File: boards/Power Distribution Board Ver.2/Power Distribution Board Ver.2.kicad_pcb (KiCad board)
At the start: 4 copper layers, 12.4 x 13.7 mm, 93 parts, among them J1 Screw_Terminal_01x02, J2 Screw_Terminal_01x06, J3 Screw_Terminal_01x06, J4 Screw_Terminal_01x06, K1 Relay, K2 Relay, K3 Relay, K4 Relay, K5 Relay, K6 Relay, SW1 SW_Push_Open, U1 SIC431AED-T1-GE3, U2 SIC431AED-T1-GE3, U3 SIC431AED-T1-GE3

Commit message: PCB update 1
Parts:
- C1, C10, C11, C12, C13, C14, C15, C16, C18, C19, C2, C20, C21, C22, C23, C24, C25, C26, C27, C28, C29, C3, C30, C31, C32, C33, C34, C35, C36, C37, C38, C39, C4, C5, C6, C7, C8, C9, J1, J2, J3, J4: moved to B.Cu
- moved D8 166.7 mm to (83.0, 137.4), turned to -90 degrees
- moved C3 157.2 mm to (44.0, 67.7), turned to -90 degrees
- moved C22 150.0 mm to (84.0, 125.7), turned to 180 degrees
- moved C23 145.5 mm to (84.0, 122.7), turned to 180 degrees
- moved C19 142.1 mm to (83.9, 119.7), turned to 180 degrees
- moved C33 138.6 mm to (44.0, 107.7), turned to 180 degrees
- moved C34 138.6 mm to (44.0, 110.7), turned to 180 degrees
- moved C37 138.6 mm to (44.0, 119.7), turned to 180 degrees
- moved C38 138.6 mm to (44.0, 122.7), turned to 180 degrees
- moved C39 138.6 mm to (44.0, 125.7), turned to 180 degrees
- moved C35 138.5 mm to (44.0, 113.7), turned to 180 degrees
- moved C36 138.5 mm to (44.0, 116.7), turned to 180 degrees
- moved C24 137.6 mm to (84.0, 116.7), turned to 180 degrees
- moved C2 135.4 mm to (64.0, 64.0), turned to -90 degrees
- moved C25 133.3 mm to (83.9, 113.7), turned to 180 degrees
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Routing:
- net /E-stop: track 0.00 -> 83.8 mm
- net /V_BAT_IN: track 0.00 -> 21.9 mm
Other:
- board size 12.4 x 13.7 mm -> 127 x 127 mm

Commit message: Edit PCB
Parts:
- C19, C20, C21, C22, C23, C24, C25, C26, C27, C28, C29, C30, C31, C32, C33, C34, C35, C36, C37, C38, C39: moved to F.Cu
- moved J2 119.2 mm to (144.8, 46.8), turned to -90 degrees
- moved J3 88.9 mm to (147.3, 139.7), turned to 180 degrees
- moved D3 63.4 mm to (134.7, 68.8), turned to 0 degrees
- moved D4 40.5 mm to (121.9, 129.9), turned to -90 degrees
- moved D2 28.9 mm to (154.9, 129.6)
- moved D5 19.7 mm to (134.7, 88.9)
- moved C1 16.5 mm to (73.7, 71.1), turned to 0 degrees
- moved D1 15.2 mm to (134.7, 50.6)
- moved K6 15.0 mm to (111.8, 117.1), turned to 180 degrees
- moved K4 13.0 mm to (127.0, 116.8), turned to 180 degrees
- moved C33 12.6 mm to (54.9, 101.6), turned to 0 degrees
- moved C34 12.6 mm to (54.9, 104.6), turned to 0 degrees
- moved C37 12.6 mm to (54.9, 113.6), turned to 0 degrees
- moved C38 12.6 mm to (54.9, 116.6), turned to 0 degrees
- moved C39 12.6 mm to (54.9, 119.6), turned to 0 degrees
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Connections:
- D7 pad 2: /5V_OUT_1 -> /5V_OUT_2
- D9 pad 2: /5V_OUT_1 -> /5V_OUT_3
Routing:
- net /V_BAT_IN: track 21.9 -> 272.3 mm
- net GND: track 0.00 -> 147.7 mm
- net /E-stop: track 83.8 -> 169.8 mm
- net Net-(D9-A): track 0.00 -> 48.7 mm
- net /12V_IN_4: track 0.00 -> 15.8 mm
- net /5V_OUT_1: track 0.00 -> 15.6 mm
- net Net-(D2-A): track 0.00 -> 14.9 mm
- net Net-(D1-A): track 0.00 -> 13.9 mm
- net /12V_IN_3: track 0.00 -> 13.7 mm
- net /12V_IN_2: track 0.00 -> 13.4 mm
- net /12V_IN_1: track 0.00 -> 12.7 mm
- net /12V_IN_5: track 0.00 -> 12.7 mm
- net /12V_IN_6: track 0.00 -> 12.3 mm
- net /V_BAT_GND: track 0.00 -> 10.2 mm
- net Net-(D3-A): track 0.00 -> 6.54 mm
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
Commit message: PCB changes
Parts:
- C15: moved to F.Cu
- moved C18 19.7 mm to (55.5, 97.0)
- moved C22 15.4 mm to (94.0, 120.0)
- moved R21 13.7 mm to (51.5, 98.0)
- moved C30 13.0 mm to (73.0, 118.5)
- moved C12 11.9 mm to (51.5, 99.0), turned to 90 degrees
- moved C28 11.6 mm to (73.0, 116.0)
- moved C31 11.6 mm to (73.0, 110.0)
- moved C32 11.6 mm to (73.0, 113.0)
- moved C21 11.6 mm to (73.0, 107.0)
- moved C27 11.5 mm to (94.5, 104.5)
- moved C20 11.2 mm to (73.0, 104.5)
- moved C24 11.1 mm to (94.4, 114.0)
- moved C26 11.1 mm to (94.4, 108.0)
- moved C25 11.1 mm to (94.5, 111.0)
- moved R9 10.8 mm to (46.0, 91.4)
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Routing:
- net GND: track 147.7 -> 251.2 mm, vias 0 -> 4
- net Net-(D8-A): track 0.00 -> 62.2 mm
- net Net-(D7-A): track 0.00 -> 47.4 mm
- net /V_BAT_IN: track 272.3 -> 294.7 mm, vias 0 -> 2
- net Net-(U3-VDD): track 0.00 -> 17.2 mm, vias 0 -> 1
- net Net-(D9-A): track 48.7 -> 62.6 mm, vias 0 -> 1
- net Net-(L3-Pad1): track 0.00 -> 12.1 mm
- net /5V_OUT_2: track 0.00 -> 11.0 mm
- net Net-(U3-FB): track 0.00 -> 7.91 mm
- net Net-(U3-PGOOD): track 0.00 -> 5.39 mm
- net Net-(U3-MODE1): track 0.00 -> 4.33 mm
- net Net-(U3-PHASE): track 0.00 -> 4.07 mm
- net Net-(U3-EN): track 0.00 -> 4.00 mm
- net Net-(U3-MODE2): track 0.00 -> 3.86 mm
- net Net-(U3-BOOT): track 0.00 -> 3.34 mm
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
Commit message: Updated GND
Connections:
- D8 pad 2: /5V_OUT_1 -> /5V_OUT_3
- D9 pad 2: /5V_OUT_3 -> /5V_OUT_1
- J1 pad 2: /V_BAT_GND -> GND
- J2 pad 2: /12V_GND_1 -> GND
- J2 pad 4: /12V_GND_2 -> GND
- J2 pad 6: /12V_GND_3 -> GND
- J3 pad 2: /12V_GND_4 -> GND
- J3 pad 4: /12V_GND_5 -> GND
- J3 pad 6: /12V_GND_6 -> GND
- J4 pad 2: /5V_GND_1 -> GND
- J4 pad 4: /5V_GND_2 -> GND
- J4 pad 6: /5V_GND_3 -> GND
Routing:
- net /V_BAT_GND: track 10.2 -> 0.00 mm
- net GND: track 251.2 -> 261.4 mm

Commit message: Design Mostly Done
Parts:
- C6: moved to F.Cu
- R12, R15, R9: moved to B.Cu
- moved R5 16.9 mm to (44.1, 93.7), turned to 0 degrees
- moved SW1 14.4 mm to (88.3, 39.4)
- moved D2 10.7 mm to (144.2, 129.6)
- moved D9 9.83 mm to (55.3, 137.2)
- moved L1 8.55 mm to (82.3, 111.7)
- moved C6 8.54 mm to (44.1, 91.1), turned to 0 degrees
- moved L2 8.49 mm to (63.0, 111.8)
- moved R24 8.21 mm to (50.8, 99.4)
- moved R15 7.71 mm to (48.3, 99.2), turned to 90 degrees
- moved R21 7.23 mm to (57.1, 102.5)
- moved K3 6.12 mm to (115.0, 62.4)
- moved K5 6.12 mm to (115.0, 82.7)
- moved K2 5.53 mm to (148.5, 116.8), turned to 180 degrees
- moved R9 4.98 mm to (48.3, 95.8), turned to 180 degrees
- moved R18 4.71 mm to (38.1, 91.4)
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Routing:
- net GND: track 261.4 -> 3.92 mm, vias 4 -> 0
- net /V_BAT_IN: track 294.7 -> 47.2 mm, vias 2 -> 0
- net Net-(D8-A): track 62.2 -> 39.2 mm
- net Net-(D9-A): track 62.6 -> 44.4 mm, vias 1 -> 0
- net /5V_OUT_3: track 0.00 -> 14.6 mm
- net Net-(D7-A): track 47.4 -> 34.9 mm
- net Net-(D2-A): track 14.9 -> 5.68 mm
- net Net-(U3-PGOOD): track 5.39 -> 13.9 mm, vias 0 -> 1
- net Net-(U3-VDD): track 17.2 -> 9.56 mm
- net /12V_IN_1: track 12.7 -> 18.9 mm
- net /12V_IN_2: track 13.4 -> 19.3 mm
- net Net-(D1-A): track 13.9 -> 8.59 mm
- net /12V_IN_3: track 13.7 -> 18.9 mm
- net Net-(L3-Pad1): track 12.1 -> 7.79 mm
- net Net-(U3-MODE2): track 3.86 -> 7.28 mm, vias 0 -> 1
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
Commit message: PCB Front/Back Design Finished
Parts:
- C13, C14, C16, C18, C4, C5: moved to F.Cu
- R10, R11, R13, R14, R7, R8: moved to B.Cu
- moved C7 16.9 mm to (89.5, 96.5), turned to 0 degrees
- moved C13 15.9 mm to (87.0, 85.7), turned to 90 degrees
- moved R21 15.2 mm to (42.0, 100.8), turned to 0 degrees
- moved R7 15.1 mm to (86.4, 93.3), turned to 90 degrees
- moved C8 14.8 mm to (68.6, 96.5), turned to 0 degrees
- moved R20 14.3 mm to (61.0, 99.1), turned to 0 degrees
- moved R4 14.1 mm to (68.6, 93.3), turned to 0 degrees
- moved C16 14.0 mm to (87.0, 100.3), turned to 0 degrees
- moved C12 13.1 mm to (38.6, 95.7), turned to -90 degrees
- moved R2 12.9 mm to (89.5, 92.7), turned to 0 degrees
- moved R10 12.8 mm to (86.4, 97.2)
- moved R11 12.5 mm to (64.8, 96.9)
- moved R17 12.4 mm to (63.5, 85.8), turned to 90 degrees
- moved C5 11.9 mm to (67.6, 89.8)
- moved C4 11.7 mm to (89.5, 89.6)
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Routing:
- net /V_BAT_IN: track 47.2 -> 111.6 mm
- net Net-(L1-Pad1): track 0.00 -> 25.3 mm
- net Net-(L2-Pad1): track 0.00 -> 24.5 mm
- net Net-(D8-A): track 39.2 -> 56.6 mm
- net Net-(L3-Pad1): track 7.79 -> 24.3 mm
- net Net-(U1-VDD): track 0.00 -> 12.9 mm, vias 0 -> 1
- net Net-(U2-VDD): track 0.00 -> 12.6 mm, vias 0 -> 1
- net Net-(D7-A): track 34.9 -> 47.1 mm
- net Net-(U1-PGOOD): track 0.00 -> 10.2 mm, vias 0 -> 1
- net Net-(U2-FB): track 0.00 -> 9.83 mm, vias 0 -> 2
- net Net-(U2-PGOOD): track 0.00 -> 9.47 mm, vias 0 -> 1
- net Net-(U1-FB): track 0.00 -> 9.26 mm, vias 0 -> 2
- net Net-(D9-A): track 44.4 -> 52.0 mm
- net Net-(U2-EN): track 0.00 -> 7.62 mm
- net Net-(U1-EN): track 0.00 -> 7.61 mm
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
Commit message: PCBPCB Circuit Design Finished
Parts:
- moved SW1 27.9 mm to (61.1, 33.4)
- moved C8 19.4 mm to (53.1, 84.9)
- moved D2 18.7 mm to (128.7, 119.1)
- moved K2 18.7 mm to (133.0, 106.3)
- moved D4 18.7 mm to (108.4, 119.1)
- moved C1 18.7 mm to (59.4, 63.2)
- moved C10 18.7 mm to (63.9, 83.5)
- moved C12 18.7 mm to (23.1, 85.2)
- moved C16 18.7 mm to (71.5, 89.8)
- moved C18 18.7 mm to (31.7, 90.3)
- moved C19 18.7 mm to (76.8, 111.3)
- moved C2 18.7 mm to (42.9, 63.0)
- moved C22 18.7 mm to (76.8, 108.5)
- moved C23 18.7 mm to (76.8, 105.7)
- moved C24 18.7 mm to (76.8, 102.9)
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- renumbered C20 to C19~C25, C27 to C26~C32, C39 to C33~C39
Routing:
- net /E-stop: track 167.2 -> 177.1 mm
- net /V_BAT_IN: track 111.6 -> 116.0 mm
- added copper zone on In1.Cu, net /V_BAT_IN
- added copper zone on B.Cu, net GND
- added copper zone on F.Cu, net GND
- added copper zone on In2.Cu, net GND

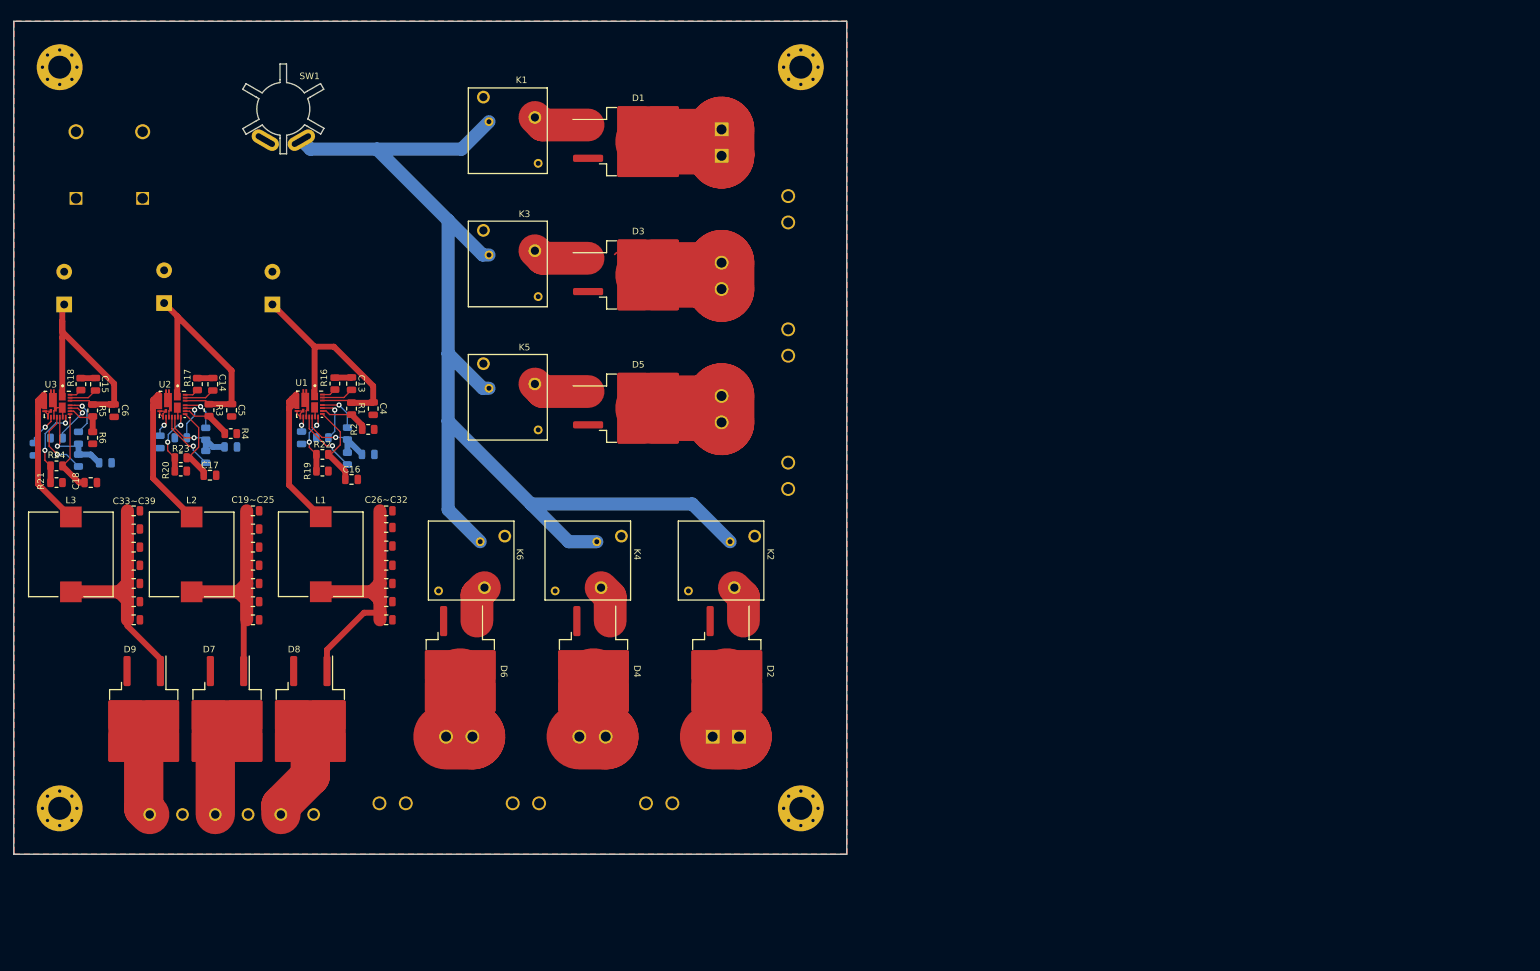
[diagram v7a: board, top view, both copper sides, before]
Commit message: Add Logo
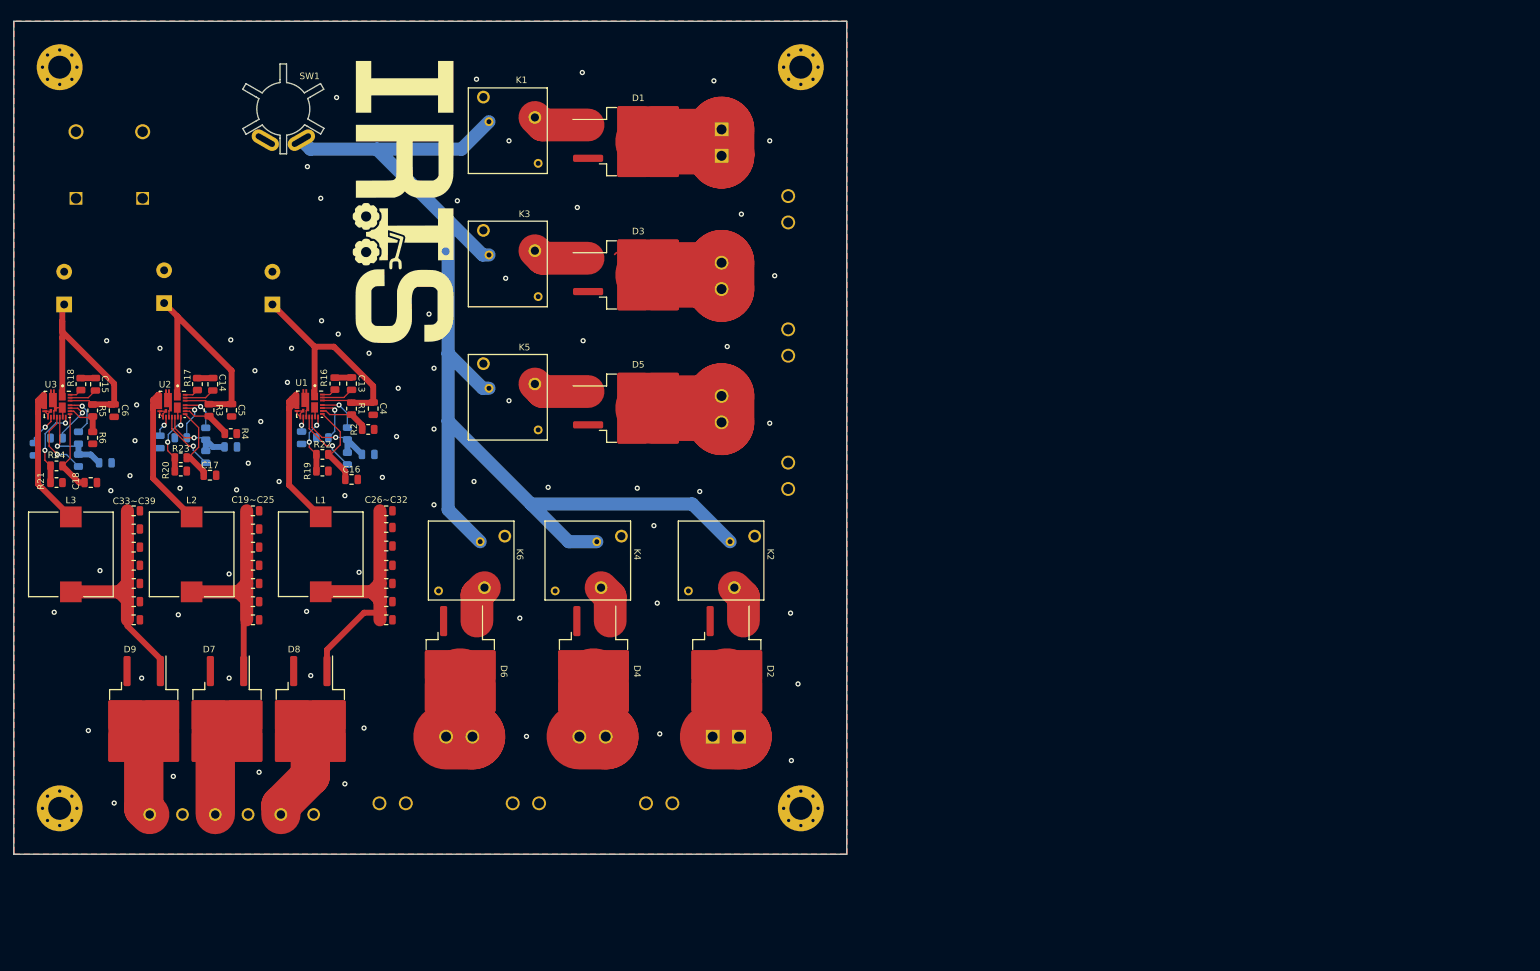
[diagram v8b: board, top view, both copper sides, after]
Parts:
- added G***: LOGO, Custom_Silkscreen_and_memes:IRIS_logo, F.Cu at (79.4, 48.4)
- added G***: LOGO, Custom_Silkscreen_and_memes:IRIS_OLD_logo, B.Cu at (49.7, 100.5)
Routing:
- net GND: vias 0 -> 71
